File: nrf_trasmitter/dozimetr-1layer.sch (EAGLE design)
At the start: 13 parts

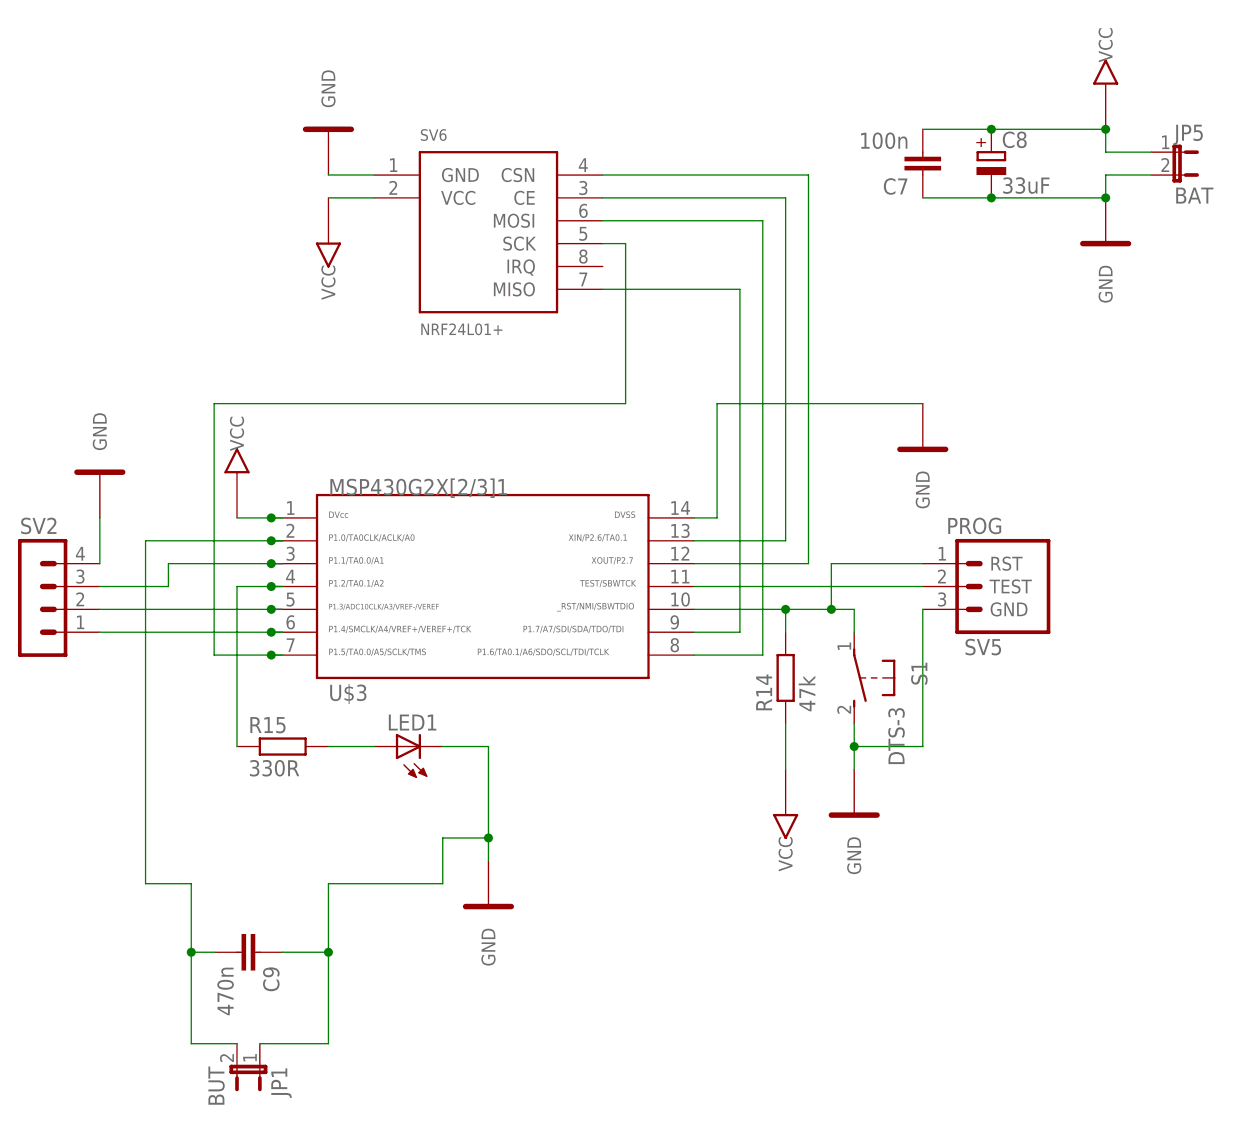
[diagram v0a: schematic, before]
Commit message: Updated nrf transmitter.
BUG: exchanged MISO and MOSI on MCU!
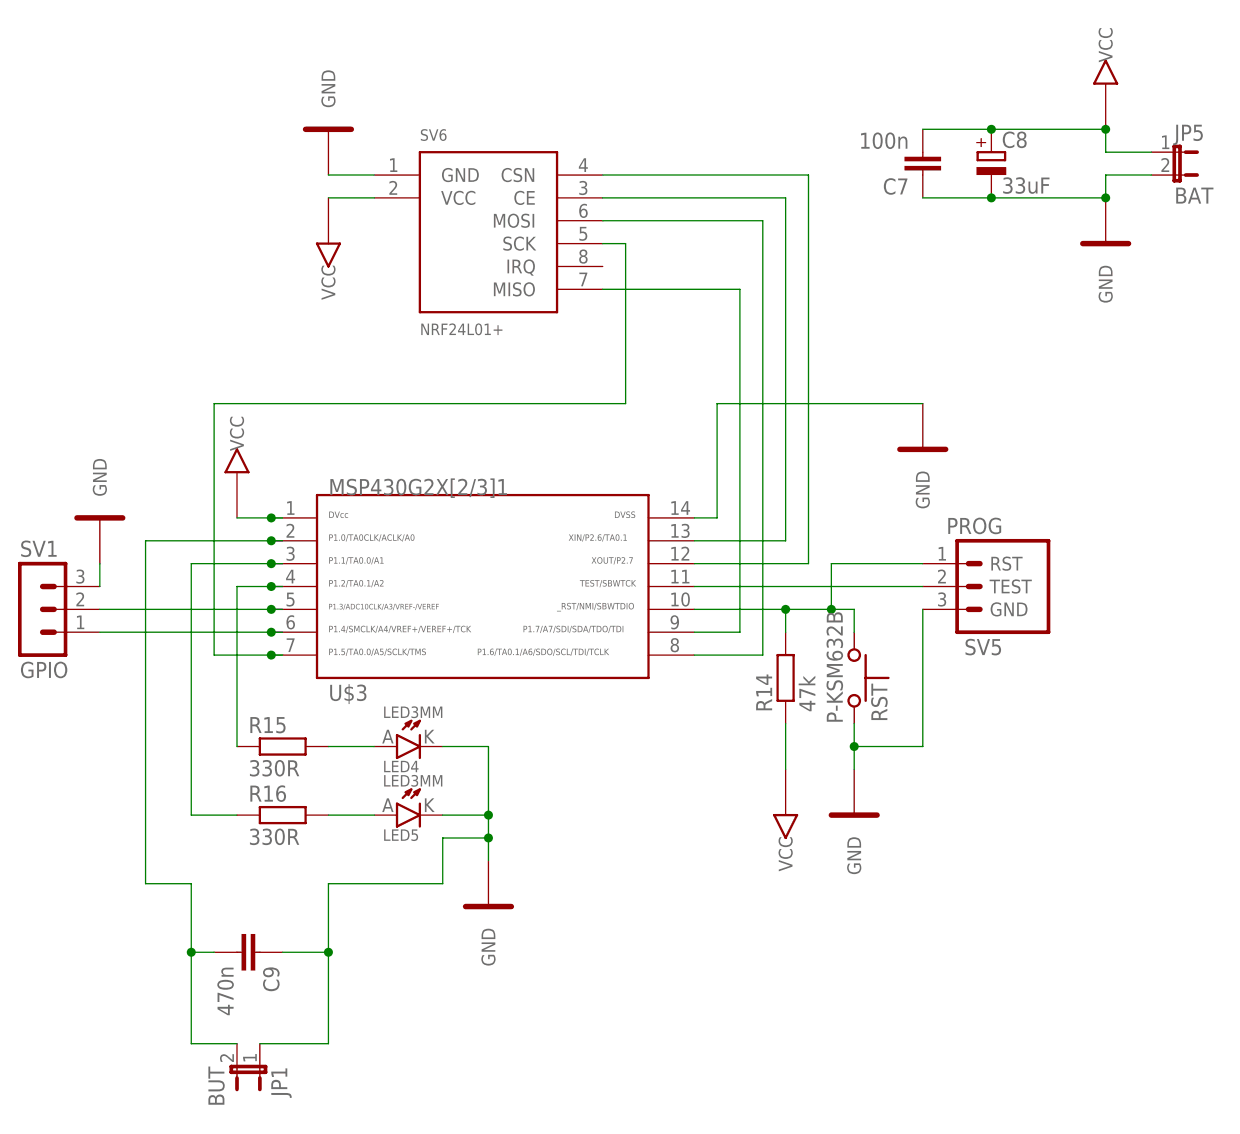
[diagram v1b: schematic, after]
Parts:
- removed LED1: (no value), led:LEDLZR181
- removed S1: DTS-3, switch-tact:DTS-3
- removed SV2: (no value), con-lstb:MA04-1
- added LED4, LED5: LED3MM, #Krakonos:LED3MM
- added R16: 330R, resistor:R-EU_R0805
- added RST: P-KSM632B, #Krakonos:P-KSM632B
- added SV1: GPIO, con-lstb:MA03-1
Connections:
- removed net N$4: SV2.3, U$3.3
- new net N$50: R16.1, U$3.3
- new net N$51: LED5.A, R16.2
- net GND: now also LED4.C, LED5.C, RST.2, SV1.3; no longer LED1.C, S1.2, SV2.4
- net N$2: now also SV1.2; no longer SV2.2
- net N$3: now also SV1.1; no longer SV2.1
- net N$40: now also RST.1; no longer S1.1
- net N$47: now also LED4.A; no longer LED1.A
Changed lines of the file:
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@@
 <part name="R14" library="resistor" deviceset="R-EU_" device="R0805" value="47k"/>
 <part name="VCC14" library="#Krakonos" deviceset="VCC" device=""/>
+<part name="RST" library="#Krakonos" deviceset="P-KSM632B" device=""/>
 <part name="GND18" library="#Krakonos" deviceset="GND" device=""/>
 <part name="VCC15" library="#Krakonos" deviceset="VCC" device=""/>
 <part name="R15" library="resistor" deviceset="R-EU_" device="R0805" value="330R"/>
+<part name="LED4" library="#Krakonos" deviceset="LED3MM" device=""/>
 <part name="GND19" library="#Krakonos" deviceset="GND" device=""/>
+<part name="R16" library="resistor" deviceset="R-EU_" device="R0805" value="330R"/>
+<part name="LED5" library="#Krakonos" deviceset="LED3MM" device=""/>
 <part name="C9" library="resistor" deviceset="C-EU" device="C0805K" value="470n"/>
 <part name="JP5" library="jumper" deviceset="JP1E" device="" value="BAT"/>
+<part name="SV1" library="con-lstb" deviceset="MA03-1" device="" value="GPIO"/>
 <part name="GND1" library="#Krakonos" deviceset="GND" device=""/>
 <part name="JP1" library="jumper" deviceset="JP1E" device="" value="BUT"/>
-<part name="LED1" library="led" deviceset="LED" device="LZR181"/>
-<part name="S1" library="switch-tact" deviceset="DTS-3" device=""/>
-<part name="SV2" library="con-lstb" deviceset="MA04-1" device=""/>
 </parts>
 <sheets>
@@
 <instance part="R14" gate="G$1" x="200.66" y="-101.6" rot="R90"/>
 <instance part="VCC14" gate="G$1" x="200.66" y="-116.84" rot="R180"/>
+<instance part="RST" gate="TLAC" x="208.28" y="-101.6" rot="R270"/>
 <instance part="GND18" gate="GND" x="236.22" y="-50.8"/>
 <instance part="VCC15" gate="G$1" x="236.22" y="-35.56"/>
 <instance part="R15" gate="G$1" x="144.78" y="-109.22"/>
+<instance part="LED4" gate="G$1" x="157.48" y="-109.22"/>
 <instance part="GND19" gate="GND" x="167.64" y="-124.46"/>
+<instance part="R16" gate="G$1" x="144.78" y="-116.84"/>
+<instance part="LED5" gate="G$1" x="157.48" y="-116.84"/>
 <instance part="C9" gate="G$1" x="142.24" y="-132.08" rot="R270"/>
 <instance part="JP5" gate="A" x="243.84" y="-43.18" rot="R270"/>
-<instance part="GND1" gate="GND" x="124.46" y="-81.28" rot="R180"/>
+<instance part="SV1" gate="G$1" x="116.84" y="-93.98"/>
+<instance part="GND1" gate="GND" x="124.46" y="-86.36" rot="R180"/>
 <instance part="JP1" gate="A" x="142.24" y="-144.78" rot="R180"/>
-<instance part="LED1" gate="G$1" x="157.48" y="-109.22" rot="R90"/>
-<instance part="S1" gate="G$1" x="208.28" y="-101.6" rot="R180"/>
-<instance part="SV2" gate="1" x="116.84" y="-91.44"/>
 </instances>
 <busses>
@@
 </segment>
 <segment>
+<pinref part="RST" gate="TLAC" pin="2"/>
 <pinref part="GND9" gate="GND" pin="GND"/>
 <wire x1="208.28" y1="-106.68" x2="208.28" y2="-109.22" width="0.1524" layer="91"/>
@@
 <wire x1="215.9" y1="-109.22" x2="208.28" y2="-109.22" width="0.1524" layer="91"/>
 <junction x="208.28" y="-109.22"/>
-<pinref part="S1" gate="G$1" pin="2"/>
 </segment>
 <segment>
@@
 </segment>
 <segment>
+<pinref part="LED4" gate="G$1" pin="C"/>
 <pinref part="GND19" gate="GND" pin="GND"/>
 <wire x1="162.56" y1="-109.22" x2="167.64" y2="-109.22" width="0.1524" layer="91"/>
-<wire x1="167.64" y1="-109.22" x2="167.64" y2="-119.38" width="0.1524" layer="91"/>
+<wire x1="167.64" y1="-109.22" x2="167.64" y2="-116.84" width="0.1524" layer="91"/>
+<pinref part="LED5" gate="G$1" pin="C"/>
+<wire x1="167.64" y1="-116.84" x2="167.64" y2="-119.38" width="0.1524" layer="91"/>
 <wire x1="167.64" y1="-119.38" x2="167.64" y2="-121.92" width="0.1524" layer="91"/>
+<wire x1="162.56" y1="-116.84" x2="167.64" y2="-116.84" width="0.1524" layer="91"/>
 <pinref part="C9" gate="G$1" pin="1"/>
 <wire x1="144.78" y1="-132.08" x2="149.86" y2="-132.08" width="0.1524" layer="91"/>
@@
 <junction x="149.86" y="-132.08"/>
 <junction x="167.64" y="-119.38"/>
-<pinref part="LED1" gate="G$1" pin="C"/>
+<junction x="167.64" y="-116.84"/>
 </segment>
 <segment>
@@
 </segment>
 <segment>
+<pinref part="SV1" gate="G$1" pin="3"/>
 <pinref part="GND1" gate="GND" pin="GND"/>
-<wire x1="124.46" y1="-83.82" x2="124.46" y2="-88.9" width="0.1524" layer="91"/>
-<pinref part="SV2" gate="1" pin="4"/>
+<wire x1="124.46" y1="-88.9" x2="124.46" y2="-91.44" width="0.1524" layer="91"/>
 </segment>
 </net>
@@
 <wire x1="200.66" y1="-96.52" x2="200.66" y2="-93.98" width="0.1524" layer="91"/>
 <wire x1="205.74" y1="-93.98" x2="208.28" y2="-93.98" width="0.1524" layer="91"/>
+<pinref part="RST" gate="TLAC" pin="1"/>
 <wire x1="208.28" y1="-93.98" x2="208.28" y2="-96.52" width="0.1524" layer="91"/>
 <junction x="200.66" y="-93.98"/>
 <junction x="205.74" y="-93.98"/>
-<pinref part="S1" gate="G$1" pin="1"/>
 </segment>
 </net>
@@
 <segment>
 <pinref part="R15" gate="G$1" pin="2"/>
+<pinref part="LED4" gate="G$1" pin="A"/>
 <wire x1="149.86" y1="-109.22" x2="154.94" y2="-109.22" width="0.1524" layer="91"/>
-<pinref part="LED1" gate="G$1" pin="A"/>
 </segment>
 </net>
@@
 <pinref part="U$3" gate="G$1" pin="12"/>
 <wire x1="203.2" y1="-88.9" x2="190.5" y2="-88.9" width="0.1524" layer="91"/>
+</segment>
+</net>
+<net name="N$50" class="0">
+<segment>
+<wire x1="144.78" y1="-88.9" x2="143.51" y2="-88.9" width="0.1524" layer="91"/>
+<wire x1="143.51" y1="-88.9" x2="134.62" y2="-88.9" width="0.1524" layer="91"/>
+<wire x1="134.62" y1="-88.9" x2="134.62" y2="-116.84" width="0.1524" layer="91"/>
+<pinref part="R16" gate="G$1" pin="1"/>
+<wire x1="134.62" y1="-116.84" x2="139.7" y2="-116.84" width="0.1524" layer="91"/>
+<pinref part="U$3" gate="G$1" pin="3"/>
+<junction x="143.51" y="-88.9"/>
+</segment>
+</net>
+<net name="N$51" class="0">
+<segment>
+<pinref part="R16" gate="G$1" pin="2"/>
+<pinref part="LED5" gate="G$1" pin="A"/>
+<wire x1="149.86" y1="-116.84" x2="154.94" y2="-116.84" width="0.1524" layer="91"/>
 </segment>
 </net>
@@
 <wire x1="143.51" y1="-93.98" x2="144.78" y2="-93.98" width="0.1524" layer="91"/>
 <junction x="143.51" y="-93.98"/>
-<pinref part="SV2" gate="1" pin="2"/>
+<pinref part="SV1" gate="G$1" pin="2"/>
 </segment>
 </net>
@@
 <wire x1="143.51" y1="-96.52" x2="144.78" y2="-96.52" width="0.1524" layer="91"/>
 <junction x="143.51" y="-96.52"/>
-<pinref part="SV2" gate="1" pin="1"/>
-</segment>
-</net>
-<net name="N$4" class="0">
-<segment>
-<wire x1="144.78" y1="-88.9" x2="143.51" y2="-88.9" width="0.1524" layer="91"/>
-<wire x1="143.51" y1="-88.9" x2="132.08" y2="-88.9" width="0.1524" layer="91"/>
-<wire x1="132.08" y1="-88.9" x2="132.08" y2="-91.44" width="0.1524" layer="91"/>
-<pinref part="SV2" gate="1" pin="3"/>
-<wire x1="132.08" y1="-91.44" x2="124.46" y2="-91.44" width="0.1524" layer="91"/>
-<pinref part="U$3" gate="G$1" pin="3"/>
-<junction x="143.51" y="-88.9"/>
-</segment>
-</net>
+<pinref part="SV1" gate="G$1" pin="1"/>
+</segment>
+</net>
